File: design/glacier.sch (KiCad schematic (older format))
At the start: 14 parts

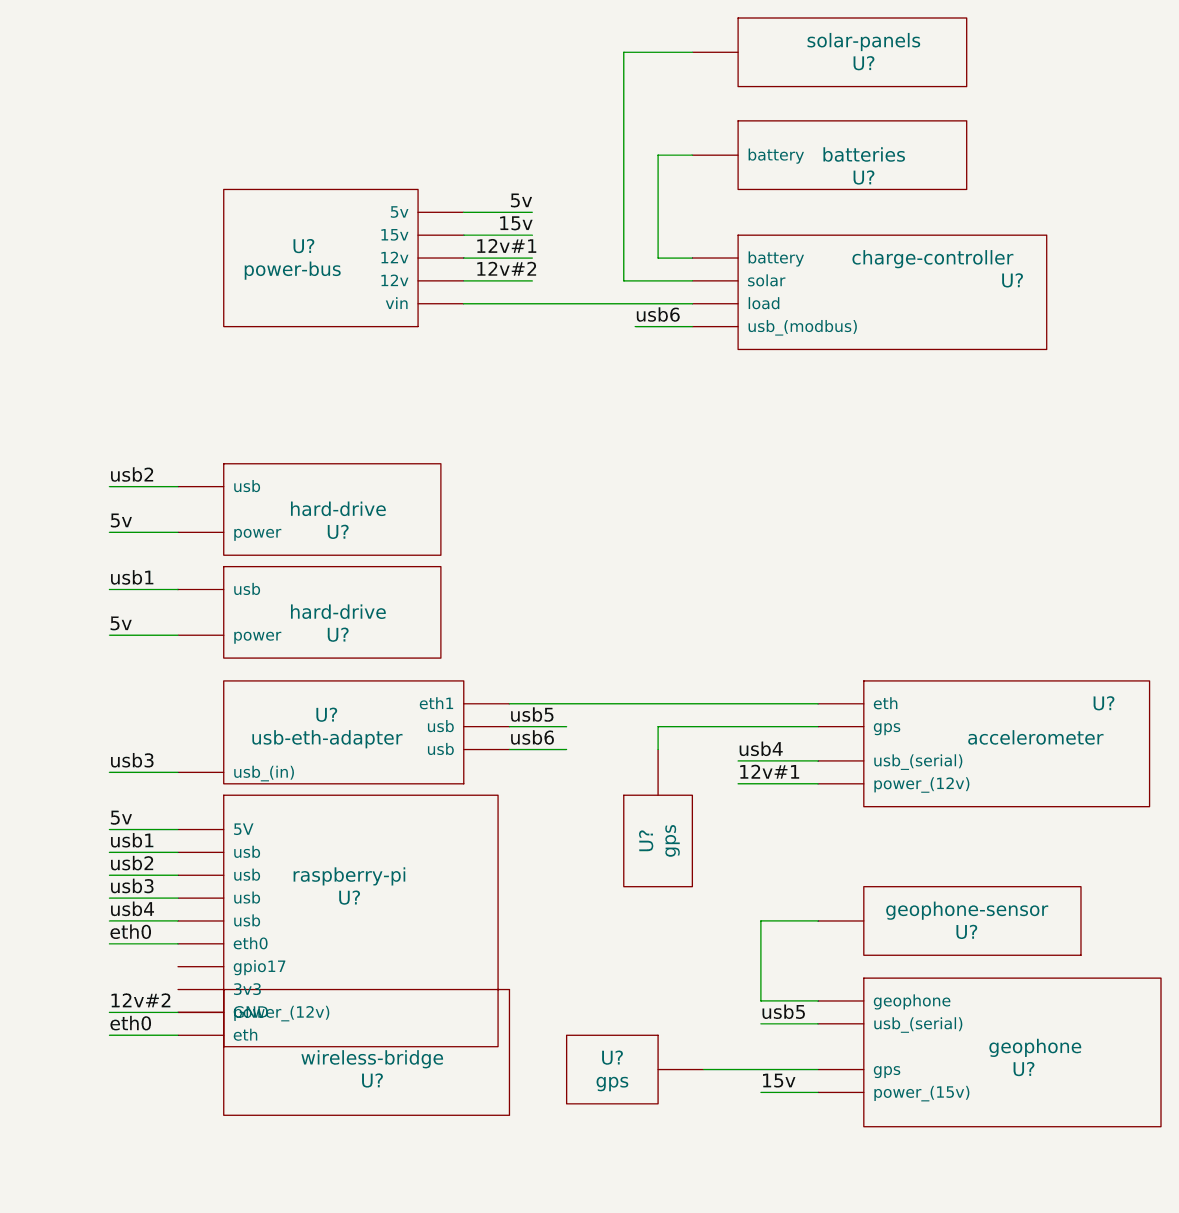
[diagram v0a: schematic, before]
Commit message: Hide component references.
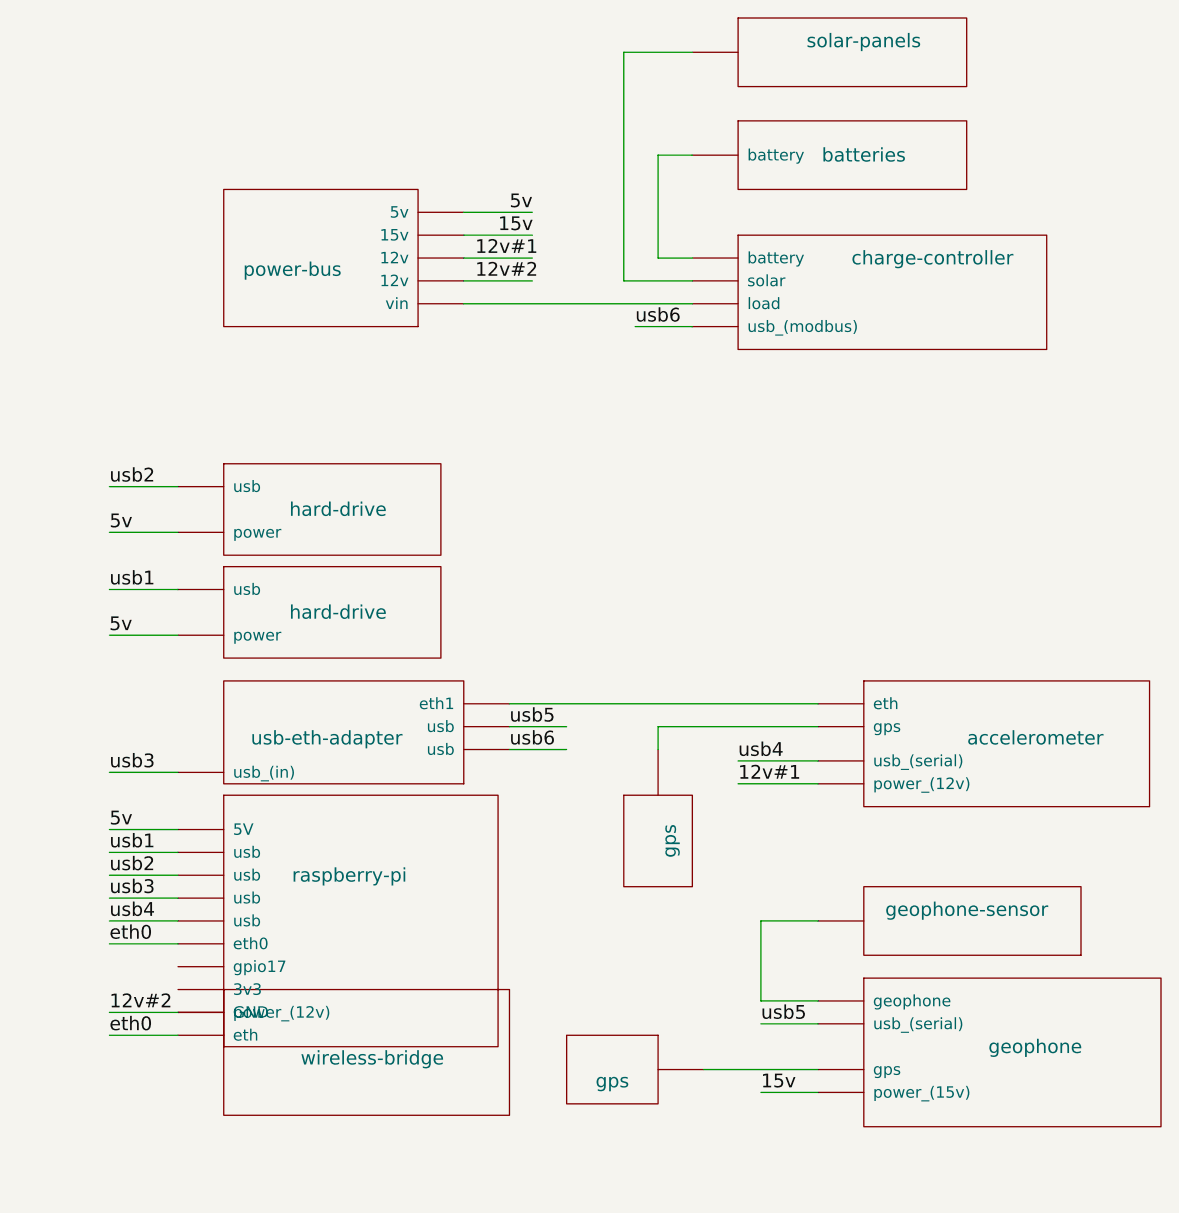
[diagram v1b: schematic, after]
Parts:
- gave numbers to parts that had none: 14
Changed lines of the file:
@@
 LIBS:valves
 LIBS:high-level
+LIBS:design-cache
 EELAYER 25 0
 EELAYER END
@@
 $EndDescr
 $Comp
-L accelerometer U?
+L accelerometer U13
 U 1 1 593F1348
 P 7450 4350
-F 0 "U?" H 7750 4500 60  0000 C CNN
+F 0 "U13" H 7750 4500 60  0001 C CNN
 F 1 "accelerometer" H 7450 4350 60  0000 C CNN
 F 2 "" H 7450 4350 60  0001 C CNN
@@
 $EndComp
 $Comp
-L charge-controller U?
+L charge-controller U12
 U 1 1 593F135F
 P 7200 2450
-F 0 "U?" H 7350 2550 60  0000 C CNN
+F 0 "U12" H 7350 2550 60  0001 C CNN
 F 1 "charge-controller" H 7000 2650 60  0000 C CNN
 F 2 "" H 7200 2450 60  0001 C CNN
@@
 $EndComp
 $Comp
-L geophone U?
+L geophone U14
 U 1 1 593F1378
 P 7450 5700
-F 0 "U?" H 7400 5600 60  0000 C CNN
+F 0 "U14" H 7400 5600 60  0001 C CNN
 F 1 "geophone" H 7450 5700 60  0000 C CNN
 F 2 "" H 7450 5700 60  0001 C CNN
@@
 $EndComp
 $Comp
-L power-bus U?
+L power-bus U1
 U 1 1 593F13B3
 P 4200 2300
-F 0 "U?" H 4150 2200 60  0000 C CNN
+F 0 "U1" H 4150 2200 60  0001 C CNN
 F 1 "power-bus" H 4200 2300 60  0000 C CNN
 F 2 "" H 4200 2300 60  0001 C CNN
@@
 $EndComp
 $Comp
-L raspberry-pi U?
+L raspberry-pi U5
 U 1 1 593F13FA
 P 4450 4950
-F 0 "U?" H 4450 4850 60  0000 C CNN
+F 0 "U5" H 4450 4850 60  0001 C CNN
 F 1 "raspberry-pi" H 4450 4950 60  0000 C CNN
 F 2 "" H 4450 4950 60  0001 C CNN
@@
 $EndComp
 $Comp
-L usb-eth-adapter U?
+L usb-eth-adapter U2
 U 1 1 593F1495
 P 4350 4350
-F 0 "U?" H 4350 4250 60  0000 C CNN
+F 0 "U2" H 4350 4250 60  0001 C CNN
 F 1 "usb-eth-adapter" H 4350 4350 60  0000 C CNN
 F 2 "" H 4350 4350 60  0001 C CNN
@@
 $EndComp
 $Comp
-L wireless-bridge U?
+L wireless-bridge U6
 U 1 1 593F1504
 P 4550 5750
-F 0 "U?" H 4550 5650 60  0000 C CNN
+F 0 "U6" H 4550 5650 60  0001 C CNN
 F 1 "wireless-bridge" H 4550 5750 60  0000 C CNN
 F 2 "" H 4550 5750 60  0001 C CNN
@@
 $EndComp
 $Comp
-L hard-drive U?
+L hard-drive U4
 U 1 1 593F15BD
 P 4400 3800
-F 0 "U?" H 4400 3700 60  0000 C CNN
+F 0 "U4" H 4400 3700 60  0001 C CNN
 F 1 "hard-drive" H 4400 3800 60  0000 C CNN
 F 2 "" H 4400 3800 60  0001 C CNN
@@
 $EndComp
 $Comp
-L hard-drive U?
+L hard-drive U3
 U 1 1 593F16E0
 P 4400 3350
-F 0 "U?" H 4400 3250 60  0000 C CNN
+F 0 "U3" H 4400 3250 60  0001 C CNN
 F 1 "hard-drive" H 4400 3350 60  0000 C CNN
 F 2 "" H 4400 3350 60  0001 C CNN
@@
 12v#1
 $Comp
-L batteries U?
+L batteries U10
 U 1 1 593F2508
 P 6700 1800
-F 0 "U?" H 6700 1700 60  0000 C CNN
+F 0 "U10" H 6700 1700 60  0001 C CNN
 F 1 "batteries" H 6700 1800 60  0000 C CNN
 F 2 "" H 6700 1800 60  0001 C CNN
@@
 	5800 4300 6500 4300
 $Comp
-L gps U?
+L gps U7
 U 1 1 593F4001
 P 5600 5800
-F 0 "U?" H 5600 5750 60  0000 C CNN
+F 0 "U7" H 5600 5750 60  0001 C CNN
 F 1 "gps" H 5600 5850 60  0000 C CNN
 F 2 "" H 5600 5850 60  0001 C CNN
@@
 $EndComp
 $Comp
-L gps U?
+L gps U8
 U 1 1 593F40B7
 P 5800 4800
-F 0 "U?" H 5800 4750 60  0000 C CNN
+F 0 "U8" H 5800 4750 60  0001 C CNN
 F 1 "gps" H 5800 4850 60  0000 C CNN
 F 2 "" H 5800 4850 60  0001 C CNN
@@
 $EndComp
 $Comp
-L geophone-sensor U?
+L geophone-sensor U11
 U 1 1 593F420B
 P 7150 5150
-F 0 "U?" H 7150 5100 60  0000 C CNN
+F 0 "U11" H 7150 5100 60  0001 C CNN
 F 1 "geophone-sensor" H 7150 5200 60  0000 C CNN
 F 2 "" H 7150 5200 60  0001 C CNN
@@
 	5700 2550 5950 2550
 $Comp
-L solar-panels U?
+L solar-panels U9
 U 1 1 593F50F1
 P 6700 1350
-F 0 "U?" H 6700 1300 60  0000 C CNN
+F 0 "U9" H 6700 1300 60  0001 C CNN
 F 1 "solar-panels" H 6700 1400 60  0000 C CNN
 F 2 "" H 6700 1400 60  0001 C CNN

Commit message: Updating hardware design docs.
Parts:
- removed U3: hard-drive, symbol hard-drive
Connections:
- wire segments 38 -> 36
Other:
- note added: "5v: 5v @ 3A \n15v: 15v @ 2A\n12v#1: 12v @ 2A\n12v#2: 12v @ 4.2A"
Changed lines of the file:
@@
 L charge-controller U12
 U 1 1 593F135F
-P 7200 2450
-F 0 "U12" H 7350 2550 60  0001 C CNN
-F 1 "charge-controller" H 7000 2650 60  0000 C CNN
-F 2 "" H 7200 2450 60  0001 C CNN
-F 3 "" H 7200 2450 60  0001 C CNN
-	1    7200 2450
+P 7200 3250
+F 0 "U12" H 7350 3350 60  0001 C CNN
+F 1 "charge-controller" H 7000 3450 60  0000 C CNN
+F 2 "" H 7200 3250 60  0001 C CNN
+F 3 "" H 7200 3250 60  0001 C CNN
+	1    7200 3250
 	1    0    0    -1
 $EndComp
@@
 L power-bus U1
 U 1 1 593F13B3
-P 4200 2300
-F 0 "U1" H 4150 2200 60  0001 C CNN
-F 1 "power-bus" H 4200 2300 60  0000 C CNN
-F 2 "" H 4200 2300 60  0001 C CNN
-F 3 "" H 4200 2300 60  0001 C CNN
-	1    4200 2300
+P 4200 3100
+F 0 "U1" H 4150 3000 60  0001 C CNN
+F 1 "power-bus" H 4200 3100 60  0000 C CNN
+F 2 "" H 4200 3100 60  0001 C CNN
+F 3 "" H 4200 3100 60  0001 C CNN
+	1    4200 3100
 	-1   0    0    1
 $EndComp
@@
 L wireless-bridge U6
 U 1 1 593F1504
-P 4550 5750
-F 0 "U6" H 4550 5650 60  0001 C CNN
-F 1 "wireless-bridge" H 4550 5750 60  0000 C CNN
-F 2 "" H 4550 5750 60  0001 C CNN
-F 3 "" H 4550 5750 60  0001 C CNN
-	1    4550 5750
+P 4550 6100
+F 0 "U6" H 4550 6000 60  0001 C CNN
+F 1 "wireless-bridge" H 4550 6100 60  0000 C CNN
+F 2 "" H 4550 6100 60  0001 C CNN
+F 3 "" H 4550 6100 60  0001 C CNN
+	1    4550 6100
 	1    0    0    -1
 $EndComp
@@
 	1    0    0    -1
 $EndComp
-$Comp
-L hard-drive U3
-U 1 1 593F16E0
-P 4400 3350
-F 0 "U3" H 4400 3250 60  0001 C CNN
-F 1 "hard-drive" H 4400 3350 60  0000 C CNN
-F 2 "" H 4400 3350 60  0001 C CNN
-F 3 "" H 4400 3350 60  0001 C CNN
-	1    4400 3350
-	1    0    0    -1
-$EndComp
-Text Label 5150 2050 0    60   ~ 0
+Text Label 5150 2850 0    60   ~ 0
 5v
-Text Label 5100 2150 0    60   ~ 0
+Text Label 5100 2950 0    60   ~ 0
 15v
-Text Label 5000 2250 0    60   ~ 0
-12v#1
-Text Label 5000 2350 0    60   ~ 0
-12v#2
 Text Label 6150 4550 0    60   ~ 0
 12v#1
@@
 L batteries U10
 U 1 1 593F2508
-P 6700 1800
-F 0 "U10" H 6700 1700 60  0001 C CNN
-F 1 "batteries" H 6700 1800 60  0000 C CNN
-F 2 "" H 6700 1800 60  0001 C CNN
-F 3 "" H 6700 1800 60  0001 C CNN
-	1    6700 1800
+P 6700 2600
+F 0 "U10" H 6700 2500 60  0001 C CNN
+F 1 "batteries" H 6700 2600 60  0000 C CNN
+F 2 "" H 6700 2600 60  0001 C CNN
+F 3 "" H 6700 2600 60  0001 C CNN
+	1    6700 2600
 	1    0    0    -1
 $EndComp
@@
 5v
 Wire Wire Line
-	3400 5650 3700 5650
+	3400 6000 3700 6000
 Wire Wire Line
 	5150 4200 6500 4200
 Wire Wire Line
-	4950 2050 5250 2050
-Wire Wire Line
-	5250 2150 4950 2150
-Wire Wire Line
-	5250 2250 4950 2250
-Wire Wire Line
-	5250 2350 4950 2350
-Wire Wire Line
-	4950 2450 5950 2450
-Wire Wire Line
-	5950 2250 5800 2250
-Wire Wire Line
-	5800 2250 5800 1800
-Wire Wire Line
-	5800 1800 5950 1800
+	4950 2850 5250 2850
+Wire Wire Line
+	5250 2950 4950 2950
+Wire Wire Line
+	4950 3250 5950 3250
+Wire Wire Line
+	5950 3050 5800 3050
+Wire Wire Line
+	5800 3050 5800 2600
+Wire Wire Line
+	5800 2600 5950 2600
 Wire Wire Line
 	3400 4750 3700 4750
@@
 Wire Wire Line
 	3400 3900 3700 3900
-Wire Wire Line
-	3400 3450 3700 3450
-Wire Wire Line
-	3400 3250 3700 3250
 Text Label 3500 3900 2    60   ~ 0
 5v
-Text Label 3400 3450 0    60   ~ 0
-5v
-Text Label 3400 3250 0    60   ~ 0
-usb2
 Text Label 3400 3700 0    60   ~ 0
 usb1
@@
 Text Label 3400 5250 0    60   ~ 0
 eth0
-Text Label 3400 5650 0    60   ~ 0
+Text Label 3400 6000 0    60   ~ 0
 eth0
 Wire Wire Line
-	3700 5550 3400 5550
-Text Label 3400 5550 0    60   ~ 0
+	3700 5900 3400 5900
+Text Label 3400 5900 0    60   ~ 0
 12v#2
 Text Label 6150 4450 0    60   ~ 0
@@
 Text Label 6250 5600 0    60   ~ 0
 usb5
-Text Label 5700 2550 0    60   ~ 0
+Text Label 5700 3350 0    60   ~ 0
 usb6
 Wire Wire Line
-	5700 2550 5950 2550
+	5700 3350 5950 3350
 $Comp
 L solar-panels U9
 U 1 1 593F50F1
-P 6700 1350
-F 0 "U9" H 6700 1300 60  0001 C CNN
-F 1 "solar-panels" H 6700 1400 60  0000 C CNN
-F 2 "" H 6700 1400 60  0001 C CNN
-F 3 "" H 6700 1400 60  0001 C CNN
-	1    6700 1350
-	1    0    0    -1
-$EndComp
-Wire Wire Line
-	5950 2350 5650 2350
-Wire Wire Line
-	5650 2350 5650 1350
-Wire Wire Line
-	5650 1350 5950 1350
+P 6700 2150
+F 0 "U9" H 6700 2100 60  0001 C CNN
+F 1 "solar-panels" H 6700 2200 60  0000 C CNN
+F 2 "" H 6700 2200 60  0001 C CNN
+F 3 "" H 6700 2200 60  0001 C CNN
+	1    6700 2150
+	1    0    0    -1
+$EndComp
+Wire Wire Line
+	5950 3150 5650 3150
+Wire Wire Line
+	5650 3150 5650 2150
+Wire Wire Line
+	5650 2150 5950 2150
+Wire Wire Line
+	5250 3150 4950 3150
+Wire Wire Line
+	5250 3050 4950 3050
+Text Label 5000 3150 0    60   ~ 0
+12v#2
+Text Label 5000 3050 0    60   ~ 0
+12v#1
+Text Notes 3000 3150 0    60   ~ 0
+5v:      5v @ 3A \n15v:    15v @ 2A\n12v#1: 12v @ 2A\n12v#2: 12v @ 4.2A
 $EndSCHEMATC
